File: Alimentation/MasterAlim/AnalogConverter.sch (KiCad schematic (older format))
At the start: 12 parts, among them U2 PCF8591

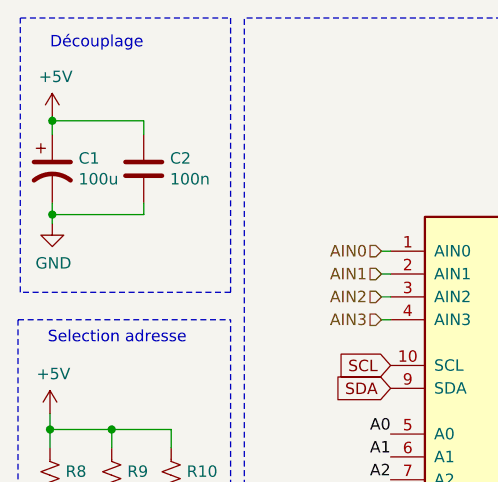
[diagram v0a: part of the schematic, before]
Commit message: Dimensionnement et récupération des part LCSC
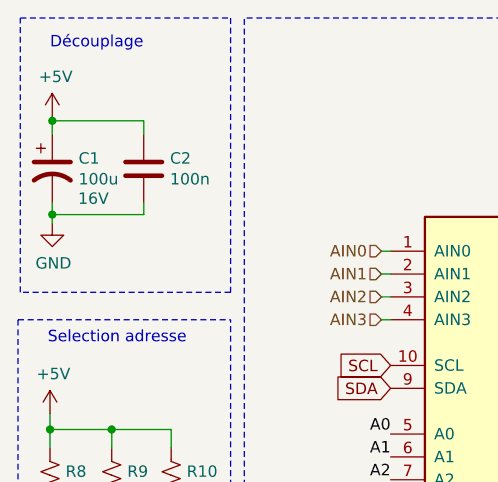
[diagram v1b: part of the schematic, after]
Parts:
- C1: footprint Capacitor_SMD:CP_Elec_3x5.3 -> Capacitor_SMD:CP_Elec_8x6.5; LCSC Part (none) -> C249832; Tension (none) -> 16V
- C2: footprint Capacitor_SMD:C_0805_2012Metric -> Capacitor_SMD:C_0805_2012Metric_Pad1.18x1.45mm_HandSolder; LCSC Part (none) -> C28233
- R10, R11, R25, R8, R9: footprint Resistor_SMD:R_0805_2012Metric -> Resistor_SMD:R_0805_2012Metric_Pad1.20x1.40mm_HandSolder
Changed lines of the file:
@@
 AR Path="/60F3E9E6/60B19B2D" Ref="#PWR0129"  Part="1"
 AR Path="/60F517CF/60B19B2D" Ref="#PWR0135"  Part="1"
-F 0 "#PWR0115" H 7320 4240 50  0001 C CNN
+F 0 "#PWR0135" H 7320 4240 50  0001 C CNN
 F 1 "GND" H 7325 4317 50  0000 C CNN
 F 2 "" H 7320 4490 50  0001 C CNN
@@
 F 0 "R11" H 7388 3316 50  0000 L CNN
 F 1 "10k" H 7388 3225 50  0000 L CNN
-F 2 "Resistor_SMD:R_0805_2012Metric" V 7360 3260 50  0001 C CNN
+F 2 "Resistor_SMD:R_0805_2012Metric_Pad1.20x1.40mm_HandSolder" V 7360 3260 50  0001 C CNN
 F 3 "~" H 7320 3270 50  0001 C CNN
 	1    7320 3270
@@
 AR Path="/60F3E9E6/60B19B45" Ref="#PWR0130"  Part="1"
 AR Path="/60F517CF/60B19B45" Ref="#PWR0136"  Part="1"
-F 0 "#PWR0117" H 6260 2600 50  0001 C CNN
+F 0 "#PWR0136" H 6260 2600 50  0001 C CNN
 F 1 "+5V" H 6275 2923 50  0000 C CNN
 F 2 "" H 6260 2750 50  0001 C CNN
@@
 AR Path="/60F3E9E6/60B5D466" Ref="#PWR0131"  Part="1"
 AR Path="/60F517CF/60B5D466" Ref="#PWR0137"  Part="1"
-F 0 "#PWR0118" H 4170 4500 50  0001 C CNN
+F 0 "#PWR0137" H 4170 4500 50  0001 C CNN
 F 1 "GND" H 4175 4577 50  0000 C CNN
 F 2 "" H 4170 4750 50  0001 C CNN
@@
 F 0 "R8" H 4238 4186 50  0000 L CNN
 F 1 "10k" H 4238 4095 50  0000 L CNN
-F 2 "Resistor_SMD:R_0805_2012Metric" V 4210 4130 50  0001 C CNN
+F 2 "Resistor_SMD:R_0805_2012Metric_Pad1.20x1.40mm_HandSolder" V 4210 4130 50  0001 C CNN
 F 3 "~" H 4170 4140 50  0001 C CNN
 	1    4170 4140
@@
 F 0 "R9" H 4508 4186 50  0000 L CNN
 F 1 "10k" H 4508 4095 50  0000 L CNN
-F 2 "Resistor_SMD:R_0805_2012Metric" V 4480 4130 50  0001 C CNN
+F 2 "Resistor_SMD:R_0805_2012Metric_Pad1.20x1.40mm_HandSolder" V 4480 4130 50  0001 C CNN
 F 3 "~" H 4440 4140 50  0001 C CNN
 	1    4440 4140
@@
 F 0 "R10" H 4768 4186 50  0000 L CNN
 F 1 "10k" H 4768 4095 50  0000 L CNN
-F 2 "Resistor_SMD:R_0805_2012Metric" V 4740 4130 50  0001 C CNN
+F 2 "Resistor_SMD:R_0805_2012Metric_Pad1.20x1.40mm_HandSolder" V 4740 4130 50  0001 C CNN
 F 3 "~" H 4700 4140 50  0001 C CNN
 	1    4700 4140
@@
 AR Path="/60F3E9E6/60B5E193" Ref="#PWR0132"  Part="1"
 AR Path="/60F517CF/60B5E193" Ref="#PWR0138"  Part="1"
-F 0 "#PWR0119" H 4170 3690 50  0001 C CNN
+F 0 "#PWR0138" H 4170 3690 50  0001 C CNN
 F 1 "+5V" H 4185 4013 50  0000 C CNN
 F 2 "" H 4170 3840 50  0001 C CNN
@@
 F 0 "C2" H 4695 2816 50  0000 L CNN
 F 1 "100n" H 4695 2725 50  0000 L CNN
-F 2 "Capacitor_SMD:C_0805_2012Metric" H 4618 2620 50  0001 C CNN
+F 2 "Capacitor_SMD:C_0805_2012Metric_Pad1.18x1.45mm_HandSolder" H 4618 2620 50  0001 C CNN
 F 3 "~" H 4580 2770 50  0001 C CNN
+F 4 "C28233" H 4580 2770 50  0001 C CNN "LCSC Part"
 	1    4580 2770
 	1    0    0    -1
@@
 F 0 "C1" H 4295 2816 50  0000 L CNN
 F 1 "100u" H 4295 2725 50  0000 L CNN
-F 2 "Capacitor_SMD:CP_Elec_3x5.3" H 4180 2770 50  0001 C CNN
+F 2 "Capacitor_SMD:CP_Elec_8x6.5" H 4180 2770 50  0001 C CNN
 F 3 "~" H 4180 2770 50  0001 C CNN
+F 4 "16V" H 4360 2640 50  0000 C CNN "Tension"
+F 5 "C249832" H 4180 2770 50  0001 C CNN "LCSC Part"
 	1    4180 2770
 	1    0    0    -1
@@
 AR Path="/60F3E9E6/60BCB48A" Ref="#PWR0133"  Part="1"
 AR Path="/60F517CF/60BCB48A" Ref="#PWR0139"  Part="1"
-F 0 "#PWR0120" H 4180 2390 50  0001 C CNN
+F 0 "#PWR0139" H 4180 2390 50  0001 C CNN
 F 1 "+5V" H 4195 2713 50  0000 C CNN
 F 2 "" H 4180 2540 50  0001 C CNN
@@
 AR Path="/60F3E9E6/60BCB490" Ref="#PWR0134"  Part="1"
 AR Path="/60F517CF/60BCB490" Ref="#PWR0140"  Part="1"
-F 0 "#PWR0121" H 4180 2760 50  0001 C CNN
+F 0 "#PWR0140" H 4180 2760 50  0001 C CNN
 F 1 "GND" H 4185 2837 50  0000 C CNN
 F 2 "" H 4180 3010 50  0001 C CNN
@@
 F 0 "R25" H 7078 4166 50  0000 L CNN
 F 1 "10k" H 7078 4075 50  0000 L CNN
-F 2 "Resistor_SMD:R_0805_2012Metric" V 7050 4110 50  0001 C CNN
+F 2 "Resistor_SMD:R_0805_2012Metric_Pad1.20x1.40mm_HandSolder" V 7050 4110 50  0001 C CNN
 F 3 "~" H 7010 4120 50  0001 C CNN
 	1    7010 4120

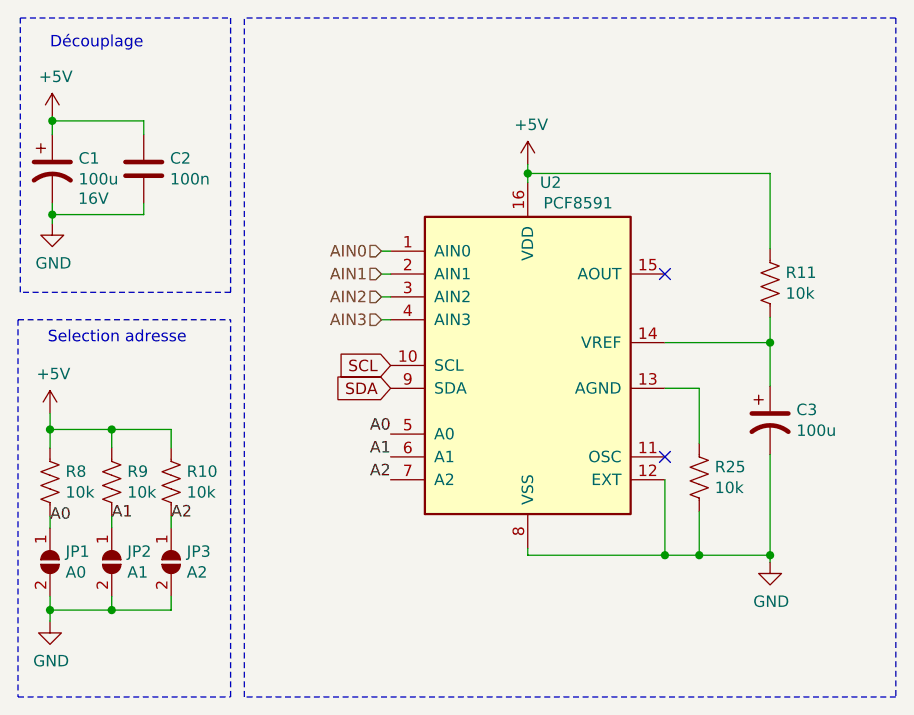
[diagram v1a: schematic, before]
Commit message: Finalisation routage carte alim maitre
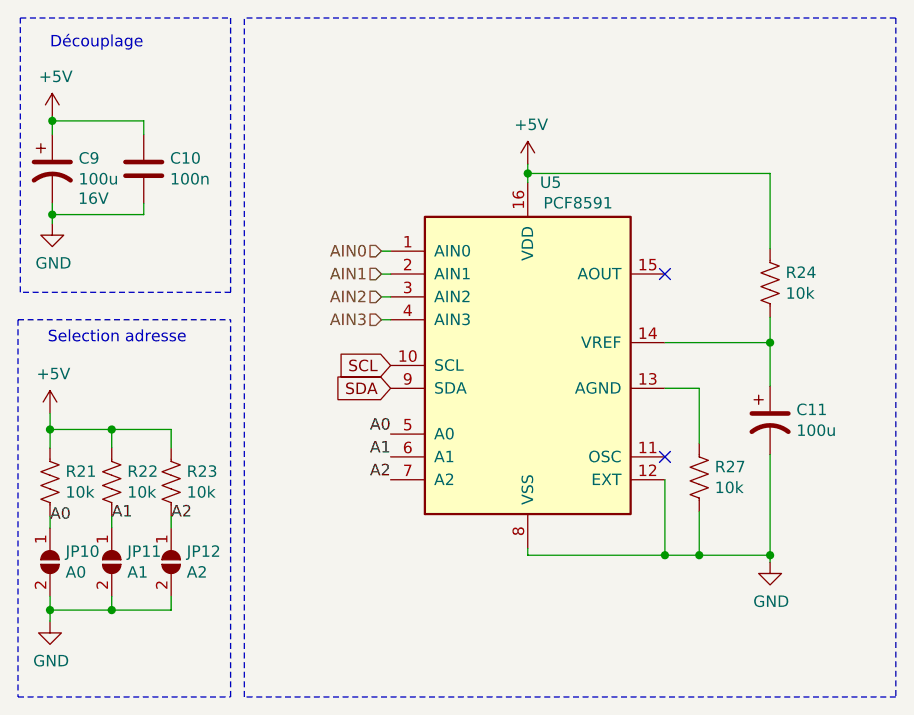
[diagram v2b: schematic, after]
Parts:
- JP1, JP2, JP3: footprint Jumper:SolderJumper-2_P1.3mm_Open_TrianglePad1.0x1.5mm -> Jumper:SolderJumper-2_P1.3mm_Open_RoundedPad1.0x1.5mm
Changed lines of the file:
@@
 $Descr A4 11693 8268
 encoding utf-8
-Sheet 2 5
+Sheet 5 5
 Title ""
 Date ""
@@
 AR Path="/60F3E9E6/60B19B19" Ref="U4"  Part="1"
 AR Path="/60F517CF/60B19B19" Ref="U5"  Part="1"
-F 0 "U2" H 6360 4430 50  0000 C CNN
+F 0 "U5" H 6360 4430 50  0000 C CNN
 F 1 "PCF8591" H 6480 4340 50  0000 C CNN
 F 2 "Package_SO:SOIC-16W_7.5x10.3mm_P1.27mm" H 6260 3430 50  0001 C CNN
@@
 AR Path="/60F3E9E6/60B19B25" Ref="C8"  Part="1"
 AR Path="/60F517CF/60B19B25" Ref="C11"  Part="1"
-F 0 "C3" H 7435 3916 50  0000 L CNN
+F 0 "C11" H 7435 3916 50  0000 L CNN
 F 1 "100u" H 7435 3825 50  0000 L CNN
 F 2 "Capacitor_SMD:CP_Elec_3x5.3" H 7320 3870 50  0001 C CNN
@@
 AR Path="/60F3E9E6/60B19B3F" Ref="R20"  Part="1"
 AR Path="/60F517CF/60B19B3F" Ref="R24"  Part="1"
-F 0 "R11" H 7388 3316 50  0000 L CNN
+F 0 "R24" H 7388 3316 50  0000 L CNN
 F 1 "10k" H 7388 3225 50  0000 L CNN
 F 2 "Resistor_SMD:R_0805_2012Metric_Pad1.20x1.40mm_HandSolder" V 7360 3260 50  0001 C CNN
@@
 AR Path="/60F3E9E6/60B5D46C" Ref="JP7"  Part="1"
 AR Path="/60F517CF/60B5D46C" Ref="JP10"  Part="1"
-F 0 "JP1" V 4124 4558 50  0000 L CNN
+F 0 "JP10" V 4124 4558 50  0000 L CNN
 F 1 "A0" V 4215 4558 50  0000 L CNN
-F 2 "Jumper:SolderJumper-2_P1.3mm_Open_TrianglePad1.0x1.5mm" H 4170 4490 50  0001 C CNN
+F 2 "Jumper:SolderJumper-2_P1.3mm_Open_RoundedPad1.0x1.5mm" H 4170 4490 50  0001 C CNN
 F 3 "~" H 4170 4490 50  0001 C CNN
 	1    4170 4490
@@
 AR Path="/60F3E9E6/60B5D472" Ref="JP8"  Part="1"
 AR Path="/60F517CF/60B5D472" Ref="JP11"  Part="1"
-F 0 "JP2" V 4394 4558 50  0000 L CNN
+F 0 "JP11" V 4394 4558 50  0000 L CNN
 F 1 "A1" V 4485 4558 50  0000 L CNN
-F 2 "Jumper:SolderJumper-2_P1.3mm_Open_TrianglePad1.0x1.5mm" H 4440 4490 50  0001 C CNN
+F 2 "Jumper:SolderJumper-2_P1.3mm_Open_RoundedPad1.0x1.5mm" H 4440 4490 50  0001 C CNN
 F 3 "~" H 4440 4490 50  0001 C CNN
 	1    4440 4490
@@
 AR Path="/60F3E9E6/60B5D478" Ref="JP9"  Part="1"
 AR Path="/60F517CF/60B5D478" Ref="JP12"  Part="1"
-F 0 "JP3" V 4654 4558 50  0000 L CNN
+F 0 "JP12" V 4654 4558 50  0000 L CNN
 F 1 "A2" V 4745 4558 50  0000 L CNN
-F 2 "Jumper:SolderJumper-2_P1.3mm_Open_TrianglePad1.0x1.5mm" H 4700 4490 50  0001 C CNN
+F 2 "Jumper:SolderJumper-2_P1.3mm_Open_RoundedPad1.0x1.5mm" H 4700 4490 50  0001 C CNN
 F 3 "~" H 4700 4490 50  0001 C CNN
 	1    4700 4490
@@
 AR Path="/60F3E9E6/60B5D486" Ref="R17"  Part="1"
 AR Path="/60F517CF/60B5D486" Ref="R21"  Part="1"
-F 0 "R8" H 4238 4186 50  0000 L CNN
+F 0 "R21" H 4238 4186 50  0000 L CNN
 F 1 "10k" H 4238 4095 50  0000 L CNN
 F 2 "Resistor_SMD:R_0805_2012Metric_Pad1.20x1.40mm_HandSolder" V 4210 4130 50  0001 C CNN
@@
 AR Path="/60F3E9E6/60B5D48C" Ref="R18"  Part="1"
 AR Path="/60F517CF/60B5D48C" Ref="R22"  Part="1"
-F 0 "R9" H 4508 4186 50  0000 L CNN
+F 0 "R22" H 4508 4186 50  0000 L CNN
 F 1 "10k" H 4508 4095 50  0000 L CNN
 F 2 "Resistor_SMD:R_0805_2012Metric_Pad1.20x1.40mm_HandSolder" V 4480 4130 50  0001 C CNN
@@
 AR Path="/60F3E9E6/60B5D492" Ref="R19"  Part="1"
 AR Path="/60F517CF/60B5D492" Ref="R23"  Part="1"
-F 0 "R10" H 4768 4186 50  0000 L CNN
+F 0 "R23" H 4768 4186 50  0000 L CNN
 F 1 "10k" H 4768 4095 50  0000 L CNN
 F 2 "Resistor_SMD:R_0805_2012Metric_Pad1.20x1.40mm_HandSolder" V 4740 4130 50  0001 C CNN
@@
 AR Path="/60F3E9E6/60BCB47E" Ref="C7"  Part="1"
 AR Path="/60F517CF/60BCB47E" Ref="C10"  Part="1"
-F 0 "C2" H 4695 2816 50  0000 L CNN
+F 0 "C10" H 4695 2816 50  0000 L CNN
 F 1 "100n" H 4695 2725 50  0000 L CNN
 F 2 "Capacitor_SMD:C_0805_2012Metric_Pad1.18x1.45mm_HandSolder" H 4618 2620 50  0001 C CNN
@@
 AR Path="/60F3E9E6/60BCB484" Ref="C6"  Part="1"
 AR Path="/60F517CF/60BCB484" Ref="C9"  Part="1"
-F 0 "C1" H 4295 2816 50  0000 L CNN
+F 0 "C9" H 4295 2816 50  0000 L CNN
 F 1 "100u" H 4295 2725 50  0000 L CNN
 F 2 "Capacitor_SMD:CP_Elec_8x6.5" H 4180 2770 50  0001 C CNN
@@
 AR Path="/60F3E9E6/5FD6079A" Ref="R26"  Part="1"
 AR Path="/60F517CF/5FD6079A" Ref="R27"  Part="1"
-F 0 "R25" H 7078 4166 50  0000 L CNN
+F 0 "R27" H 7078 4166 50  0000 L CNN
 F 1 "10k" H 7078 4075 50  0000 L CNN
 F 2 "Resistor_SMD:R_0805_2012Metric_Pad1.20x1.40mm_HandSolder" V 7050 4110 50  0001 C CNN

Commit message: Module alim ISO, clean master alim
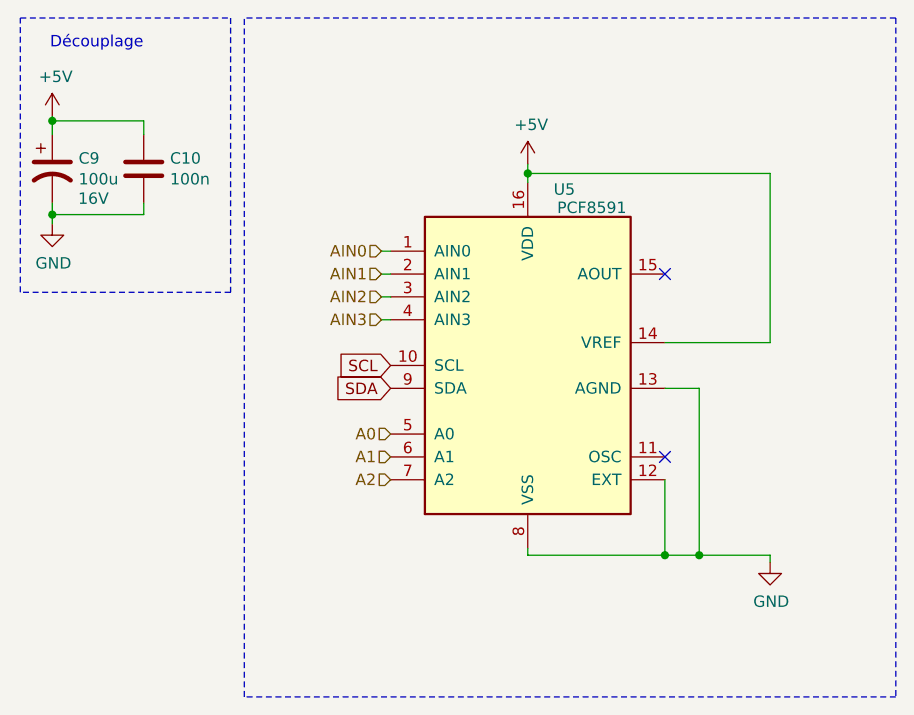
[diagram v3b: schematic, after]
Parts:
- removed C3: 100u, Capacitor_SMD:CP_Elec_3x5.3, symbol Device:CP1
- removed JP1: A0, Jumper:SolderJumper-2_P1.3mm_Open_RoundedPad1.0x1.5mm, symbol Jumper:SolderJumper_2_Open
- removed JP2: A1, Jumper:SolderJumper-2_P1.3mm_Open_RoundedPad1.0x1.5mm, symbol Jumper:SolderJumper_2_Open
- removed JP3: A2, Jumper:SolderJumper-2_P1.3mm_Open_RoundedPad1.0x1.5mm, symbol Jumper:SolderJumper_2_Open
- removed R10, R11, R25, R8, R9: 10k, Resistor_SMD:R_0805_2012Metric_Pad1.20x1.40mm_HandSolder, symbol Device:R_US
- removed U2: PCF8591, Package_SO:SOIC-16W_7.5x10.3mm_P1.27mm, symbol Interface_Expansion:PCF8591
- added U2: PCF8591, Package_SO:SOIC-16W_7.5x10.3mm_P1.27mm, symbol ARIG:PCF8591
- C2: footprint Capacitor_SMD:C_0805_2012Metric_Pad1.18x1.45mm_HandSolder -> Capacitor_SMD:C_0603_1608Metric_Pad1.08x0.95mm_HandSolder; LCSC Part C28233 -> C80516; Tension (none) -> 16V
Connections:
- net +5V: now also U2.14 (VREF), U2.16 (VDD)
- net A0: now also U2.5 (A0)
- net A1: now also U2.6 (A1)
- net A2: now also U2.7 (A2)
- net AIN0: now also U2.1 (AIN0)
- net AIN1: now also U2.2 (AIN1)
- net AIN2: now also U2.3 (AIN2)
- net AIN3: now also U2.4 (AIN3)
- net GND: now also U2.12 (EXT), U2.13 (AGND), U2.8 (VSS)
- net SCL: now also U2.10 (SCL)
- net SDA: now also U2.9 (SDA)
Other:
- note removed: "Selection adresse"
